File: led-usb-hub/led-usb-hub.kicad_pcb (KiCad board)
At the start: 4 copper layers, 127 x 50.8 mm, 138 parts, among them J1 USBC_USB2.0, J2 RGBUSB_54-00266, J3 RGBUSB_54-00266, J4 RGBUSB_54-00266, J5 SWD, SW1 RESET, SW2 BOOLSEL, SW3 LED_EN, U1 RP2040, U10 TPD2EUSB30, U11 TPD2EUSB30, U12 TC54VN3002, U13 W25Q16JVSN, U2 TPS2042D, U3 TPS2042D, U4 TPS563257DRLR, U5 TPS563257DRLR, U6 TUSB2046IBVF, U7 TPD2EUSB30, U8 TPD2EUSB30, U9 TPD2EUSB30, Y1 12Mhz, Y2 6Mhz

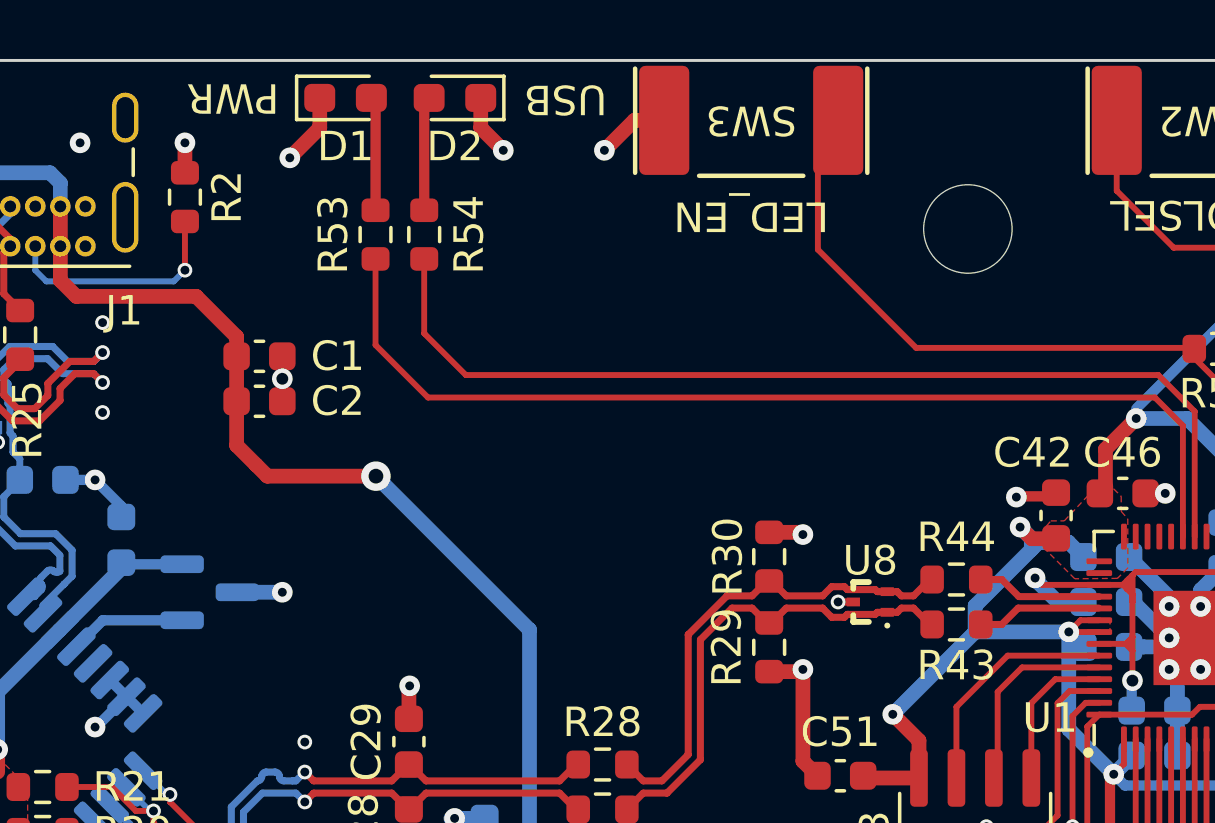
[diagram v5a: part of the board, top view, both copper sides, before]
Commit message: Fix Values for LED Resistors, add Test Points
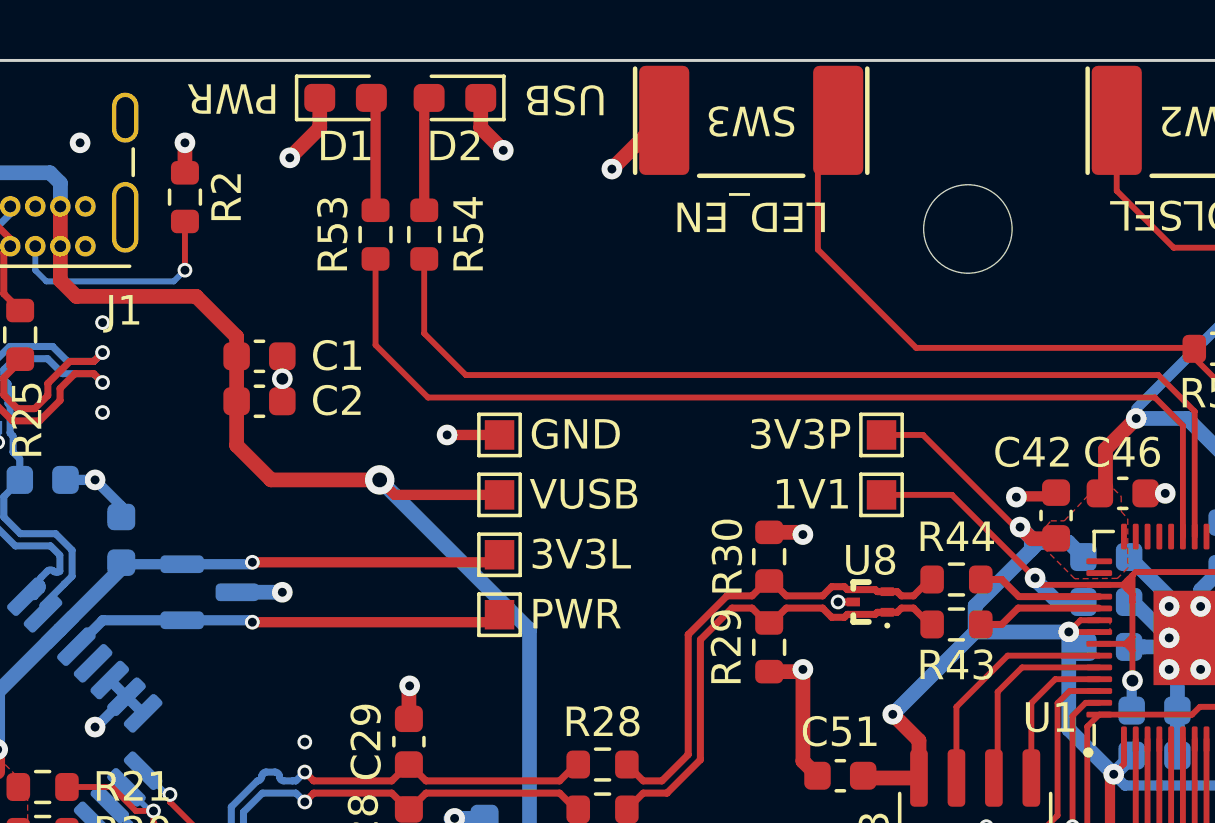
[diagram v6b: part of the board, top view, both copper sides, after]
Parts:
- added TP1: VUSB, TestPoint:TestPoint_Pad_1.0x1.0mm_Mod, F.Cu at (114.0, 96.5)
- added TP2: 3V3P, TestPoint:TestPoint_Pad_1.0x1.0mm_Mod, F.Cu at (127.0, 94.5)
- added TP3: 3V3L, TestPoint:TestPoint_Pad_1.0x1.0mm_Mod, F.Cu at (114.0, 98.6)
- added TP4: PWR, TestPoint:TestPoint_Pad_1.0x1.0mm_Mod, F.Cu at (114.0, 100.6)
- added TP5: 1V1, TestPoint:TestPoint_Pad_1.0x1.0mm_Mod, F.Cu at (127.0, 96.5)
- added TP6: GND, TestPoint:TestPoint_Pad_1.0x1.0mm_Mod, F.Cu at (114.0, 94.5)
- R10, R11, R4, R5, R7, R8: value 14 -> 30
- R3, R6, R9: value 80 -> 130
- R53, R54: value 80 -> 300
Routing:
- net 3V3_L: track 46.9 -> 57.8 mm, vias 3 -> 4
- net PWR_ON: track 3.95 -> 14.9 mm, vias 0 -> 1
- net 1V1: track 24.3 -> 30.4 mm
- net 3V3_PI: track 222.9 -> 228.7 mm
- net VUSB: track 127.8 -> 132.2 mm
- net Earth: track 138.4 -> 140.2 mm, vias 64 -> 65

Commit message: More clean up
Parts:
- moved C33 7.81 mm to (86.2, 113.9)
- moved C32 7.79 mm to (83.2, 113.9)
- moved C34 7.30 mm to (68.8, 110.7)
- moved C35 7.30 mm to (68.8, 113.7)
- moved R39 3.55 mm to (63.2, 111.5)
- moved R40 3.55 mm to (63.2, 113.0)
- moved R35 1.21 mm to (83.9, 116.2)
- moved R36 1.21 mm to (85.5, 116.2)
- moved R37 0.25 mm to (88.4, 120.6)
- moved R38 0.25 mm to (88.4, 117.5)
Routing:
- net Earth: track 140.2 -> 135.5 mm
- net U3-: track 29.2 -> 25.4 mm
- net U3+: track 29.2 -> 25.4 mm
- net /U3'-: track 28.3 -> 31.7 mm
- net /U3'+: track 28.2 -> 31.7 mm
- net PWR2: track 25.7 -> 28.1 mm
- net OC2: track 87.6 -> 89.9 mm
- net PWR3: track 24.9 -> 26.6 mm
- net 3V3_L: track 57.8 -> 56.1 mm
- net OC3: track 92.0 -> 93.5 mm
- net U2+: track 16.4 -> 17.8 mm
- net U2-: track 16.5 -> 17.8 mm
- net /U2'+: track 14.6 -> 15.7 mm
- net /U2'-: track 14.6 -> 15.6 mm
- net Net-(U1-GPIO21): track 25.6 -> 24.6 mm
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
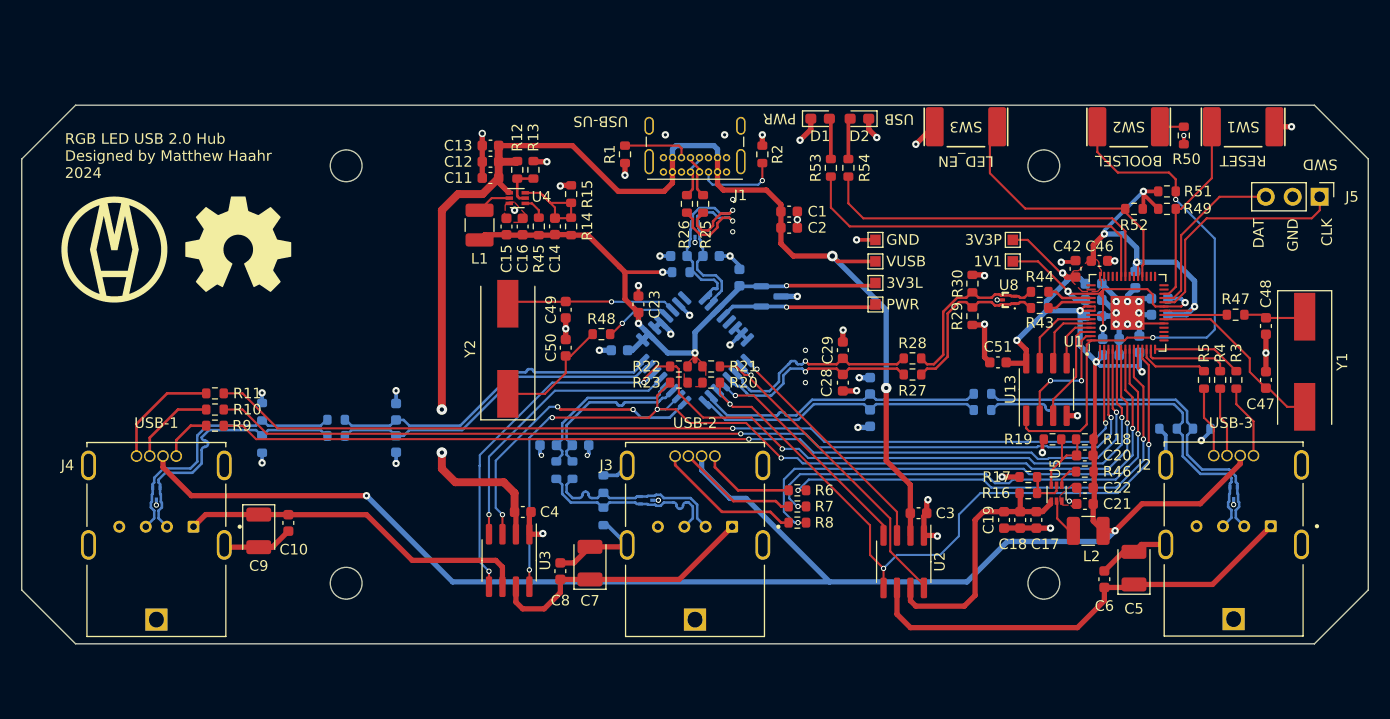
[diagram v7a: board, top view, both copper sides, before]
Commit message: Update documentation with current designs and continue clean up
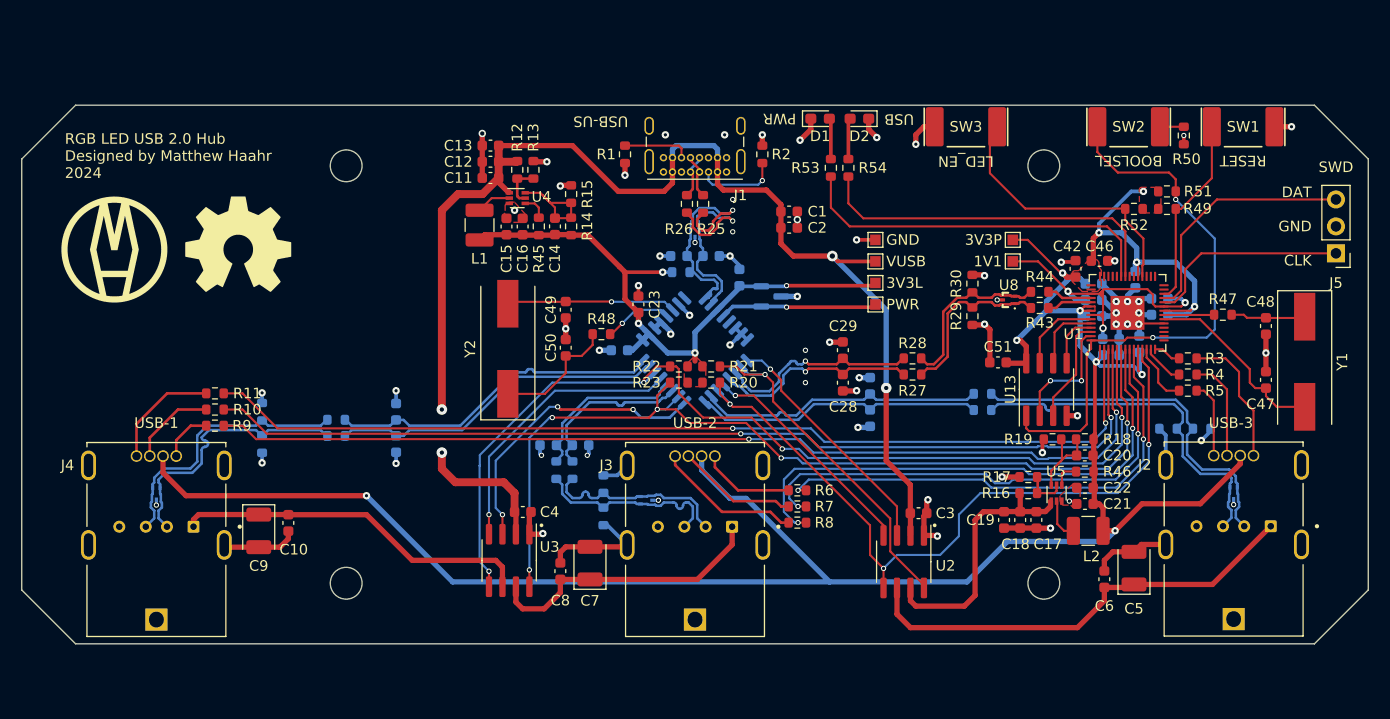
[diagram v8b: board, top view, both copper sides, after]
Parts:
- moved J5 5.55 mm to (157.5, 95.8), turned to 180 degrees
- moved R3 5.00 mm to (143.5, 105.7), turned to 0 degrees
- moved R4 3.09 mm to (143.5, 107.2), turned to 0 degrees
- moved R5 1.83 mm to (143.5, 108.7), turned to 0 degrees
- moved R47 1.21 mm to (146.8, 101.5)
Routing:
- net /SWDIO: track 16.6 -> 23.1 mm
- net Net-(J2-PadR): track 6.99 -> 13.0 mm
- net L1_R: track 8.52 -> 2.62 mm
- net L1_G: track 8.20 -> 3.92 mm
- net Net-(J2-PadG): track 6.58 -> 9.69 mm
- net /SWCLK: track 22.4 -> 19.4 mm
- net Earth: track 135.5 -> 137.8 mm
- net OC0: track 31.1 -> 33.2 mm
- net 3V3_PI: track 228.3 -> 226.3 mm
- net Net-(C48-Pad1): track 5.28 -> 6.90 mm
- net Net-(U1-XOUT): track 5.91 -> 4.74 mm
- net 5V_2: track 26.0 -> 27.0 mm
- net L1_B: track 6.72 -> 5.88 mm
- net PWR0: track 22.4 -> 23.1 mm
- net Net-(C50-Pad1): track 11.3 -> 11.9 mm
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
